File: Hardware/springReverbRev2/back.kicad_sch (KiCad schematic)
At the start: 55 parts, among them IC102 TL074, IC103 TL074, J901 AudioJack2_SwitchT, J902 AudioJack2, J903 AudioJack2, J904 AudioJack2, J905 AudioJack2_SwitchT, J906 AudioJack2, J917 DIP-8, J919 DIP-14, J920 DIP-14, U7 NE5532, U901 L78L05_TO92, X101 RCA, X102 RCA

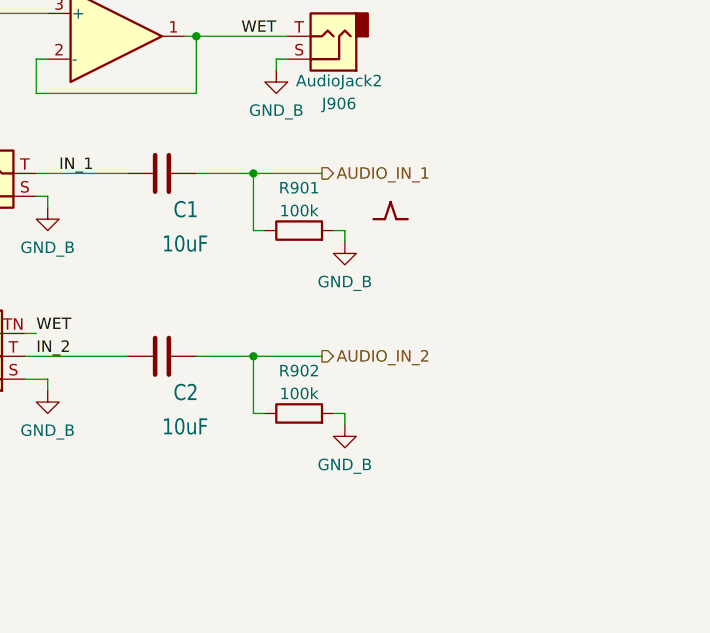
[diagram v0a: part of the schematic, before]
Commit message: Restore R4 and R5 references; change C1 and C2 values; mark R5 to omit; README list of changes
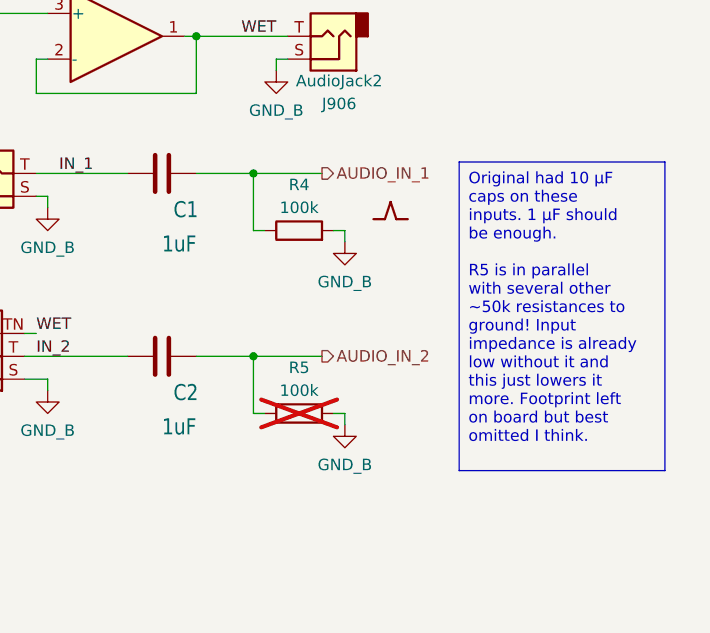
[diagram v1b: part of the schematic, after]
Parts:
- C1, C2: value 10uF -> 1uF; footprint AO_tht:C_Radial_D8.0mm_H11.5mm_P3.50mm -> AO_tht:C_Rect_L7.2mm_W7.2mm_P5.00mm_FKS2_FKP2_MKS2_MKP2
- R5: renamed from R902; now not fitted
- renumbered R901 to R4
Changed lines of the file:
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@@
     (fill (type none))
+  )
+  (text_box "Original had 10 µF caps on these inputs. 1 µF should be enough.\n\nR5 is in parallel with several other ~50k resistances to ground! Input impedance is already low without it and this just lowers it more. Footprint left on board but best omitted I think."
+    (at 243.84 135.89 0) (size 22.86 34.29)
+    (stroke (width 0) (type default))
+    (fill (type none))
+    (effects (font (size 1.27 1.27)) (justify left top))
   )
   (text "Reverb Board" (at 177.8 26.67 0)
@@
   )
   (symbol (lib_id "AO_symbols:R") (at 226.06 163.83 90) (unit 1)
-    (in_bom yes) (on_board yes) (dnp no) (fields_autoplaced)
-    (property "Reference" "R902" (at 226.06 159.1142 90)
-      (effects (font (size 1.27 1.27)))
-    )
-    (property "Value" "100k" (at 226.06 161.6511 90)
+    (in_bom yes) (on_board yes) (dnp yes) (fields_autoplaced)
+    (property "Reference" "R5" (at 226.06 158.75 90)
+      (effects (font (size 1.27 1.27)))
+    )
+    (property "Value" "100k" (at 226.06 161.29 90)
       (effects (font (size 1.27 1.27)))
     )
@@
       (project "springReverbRev2"
         (path "/7cc2117a-75f3-473b-aa3c-f6f0c8514e37/cb7e7ca4-1a75-4992-9aba-d7df48630a9d"
-          (reference "R902") (unit 1)
+          (reference "R5") (unit 1)
         )
       )
@@
     )
   )
-  (symbol (lib_id "AO_symbols:C") (at 210.82 157.48 270) (unit 1)
-    (in_bom yes) (on_board yes) (dnp no)
-    (property "Reference" "C2" (at 212.09 162.56 90)
-      (effects (font (size 1.778 1.5113)) (justify left bottom))
-    )
-    (property "Value" "10uF" (at 210.82 166.37 90)
-      (effects (font (size 1.778 1.5113)) (justify left bottom))
-    )
-    (property "Footprint" "AO_tht:C_Radial_D8.0mm_H11.5mm_P3.50mm" (at 207.01 158.4452 0)
-      (effects (font (size 1.27 1.27)) hide)
-    )
-    (property "Datasheet" "" (at 210.82 157.48 0)
-      (effects (font (size 1.27 1.27)) hide)
-    )
-    (property "Vendor" "Tayda" (at 210.82 157.48 0)
-      (effects (font (size 1.27 1.27)) hide)
-    )
-    (property "Description" "Unpolarized electrolytic capacitor" (at 210.82 157.48 0)
-      (effects (font (size 1.27 1.27)) hide)
-    )
-    (property "Manufacturer" "" (at 210.82 157.48 0)
-      (effects (font (size 1.27 1.27)) hide)
-    )
-    (property "Part" "" (at 210.82 157.48 0)
-      (effects (font (size 1.27 1.27)) hide)
-    )
-    (pin "1")
-    (pin "2")
-    (instances
-      (project "springReverbRev2"
-        (path "/7cc2117a-75f3-473b-aa3c-f6f0c8514e37/cb7e7ca4-1a75-4992-9aba-d7df48630a9d"
-          (reference "C2") (unit 1)
-        )
-      )
-    )
-  )
   (symbol (lib_id "aaaSpringReverb:GND_B") (at 39.37 187.96 0) (unit 1)
     (in_bom yes) (on_board yes) (dnp no) (fields_autoplaced)
@@
       (effects (font (size 1.778 1.5113)) (justify left bottom))
     )
-    (property "Value" "10uF" (at 210.82 146.05 90)
+    (property "Value" "1uF" (at 210.82 146.05 90)
       (effects (font (size 1.778 1.5113)) (justify left bottom))
     )
-    (property "Footprint" "AO_tht:C_Radial_D8.0mm_H11.5mm_P3.50mm" (at 207.01 138.1252 0)
+    (property "Footprint" "AO_tht:C_Rect_L7.2mm_W7.2mm_P5.00mm_FKS2_FKP2_MKS2_MKP2" (at 207.01 138.1252 0)
       (effects (font (size 1.27 1.27)) hide)
     )
@@
     )
   )
+  (symbol (lib_id "AO_symbols:C") (at 210.82 157.48 270) (unit 1)
+    (in_bom yes) (on_board yes) (dnp no)
+    (property "Reference" "C2" (at 212.09 162.56 90)
+      (effects (font (size 1.778 1.5113)) (justify left bottom))
+    )
+    (property "Value" "1uF" (at 210.82 166.37 90)
+      (effects (font (size 1.778 1.5113)) (justify left bottom))
+    )
+    (property "Footprint" "AO_tht:C_Rect_L7.2mm_W7.2mm_P5.00mm_FKS2_FKP2_MKS2_MKP2" (at 207.01 158.4452 0)
+      (effects (font (size 1.27 1.27)) hide)
+    )
+    (property "Datasheet" "" (at 210.82 157.48 0)
+      (effects (font (size 1.27 1.27)) hide)
+    )
+    (property "Vendor" "Tayda" (at 210.82 157.48 0)
+      (effects (font (size 1.27 1.27)) hide)
+    )
+    (property "Description" "Unpolarized electrolytic capacitor" (at 210.82 157.48 0)
+      (effects (font (size 1.27 1.27)) hide)
+    )
+    (property "Manufacturer" "" (at 210.82 157.48 0)
+      (effects (font (size 1.27 1.27)) hide)
+    )
+    (property "Part" "" (at 210.82 157.48 0)
+      (effects (font (size 1.27 1.27)) hide)
+    )
+    (pin "1")
+    (pin "2")
+    (instances
+      (project "springReverbRev2"
+        (path "/7cc2117a-75f3-473b-aa3c-f6f0c8514e37/cb7e7ca4-1a75-4992-9aba-d7df48630a9d"
+          (reference "C2") (unit 1)
+        )
+      )
+    )
+  )
   (symbol (lib_id "aaaSpringReverb:GND_B") (at 198.12 161.29 0) (unit 1)
     (in_bom yes) (on_board yes) (dnp no) (fields_autoplaced)
@@
   (symbol (lib_id "AO_symbols:R") (at 226.06 143.51 90) (unit 1)
     (in_bom yes) (on_board yes) (dnp no) (fields_autoplaced)
-    (property "Reference" "R901" (at 226.06 138.7942 90)
-      (effects (font (size 1.27 1.27)))
-    )
-    (property "Value" "100k" (at 226.06 141.3311 90)
+    (property "Reference" "R4" (at 226.06 138.43 90)
+      (effects (font (size 1.27 1.27)))
+    )
+    (property "Value" "100k" (at 226.06 140.97 90)
       (effects (font (size 1.27 1.27)))
     )
@@
       (project "springReverbRev2"
         (path "/7cc2117a-75f3-473b-aa3c-f6f0c8514e37/cb7e7ca4-1a75-4992-9aba-d7df48630a9d"
-          (reference "R901") (unit 1)
-        )
-      )
+          (reference "R4") (unit 1)
+        )
+      )

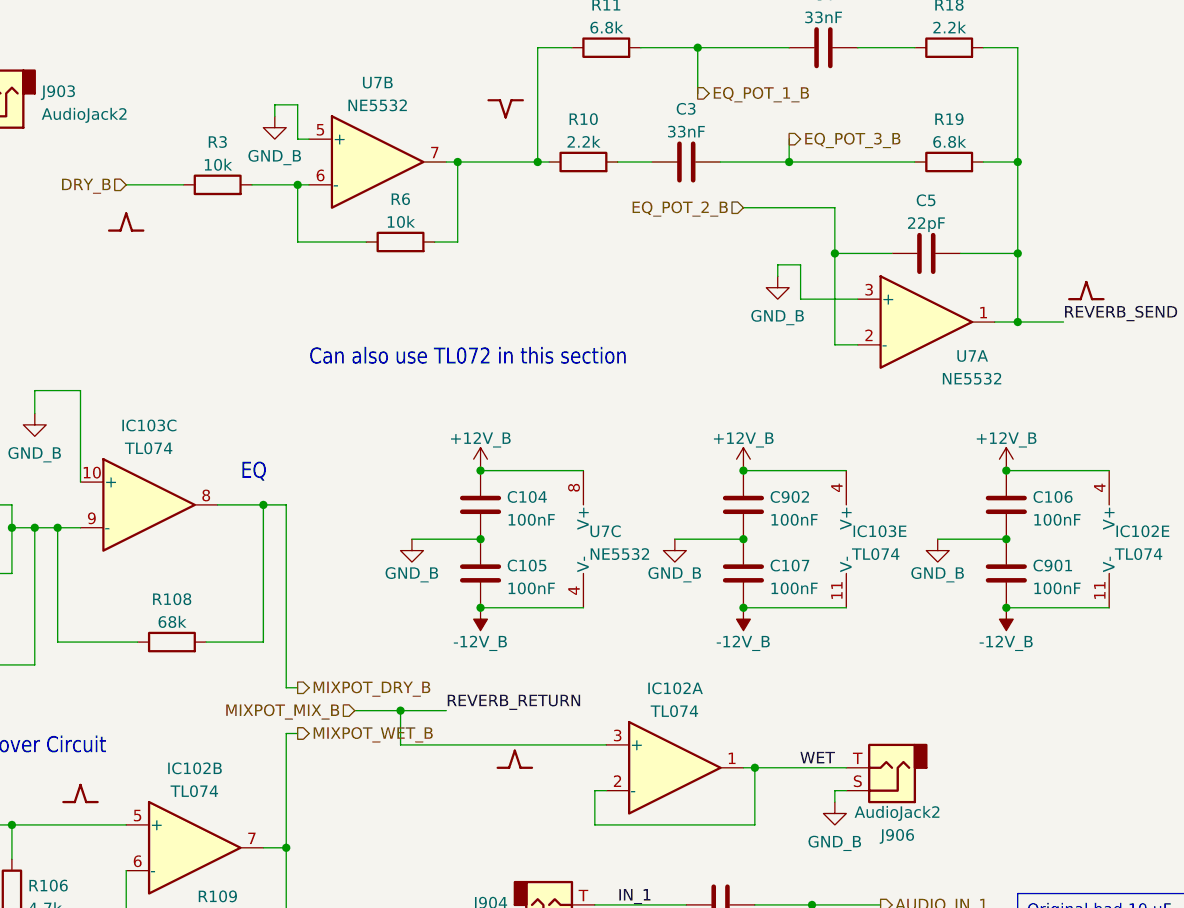
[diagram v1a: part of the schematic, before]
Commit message: Docs; make LED position consistent
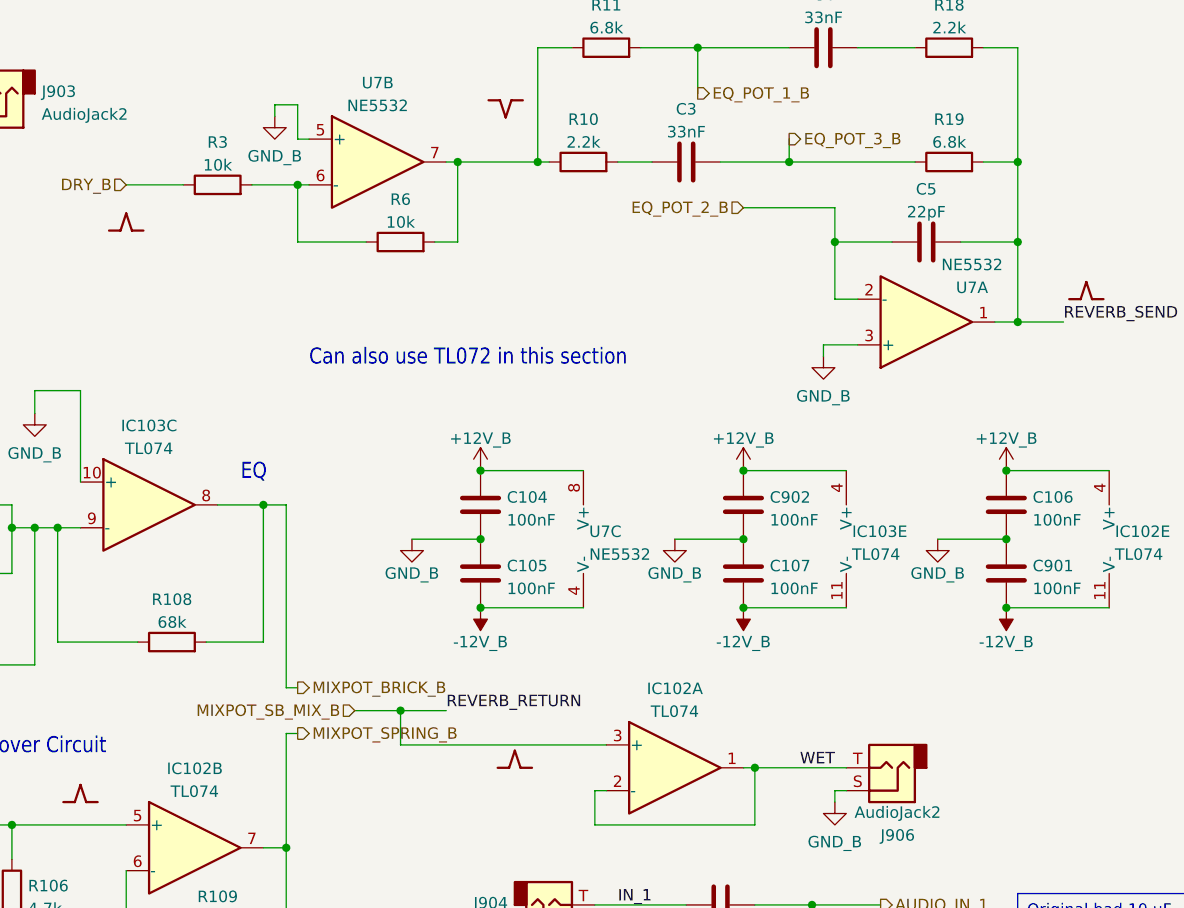
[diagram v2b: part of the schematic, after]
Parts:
- Z$102: Manufacturer (none) -> Belton Accutronics; Part (none) -> BTDR-2H
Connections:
- net MIXPOT_DRY_B renamed MIXPOT_BRICK_B
- net MIXPOT_MIX_B renamed MIXPOT_SB_MIX_B
- net MIXPOT_WET_B renamed MIXPOT_SPRING_B
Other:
- moved on the sheet: C5

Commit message: Use open not bridged jumper
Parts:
- SJ101: footprint Jumper:SolderJumper-2_P1.3mm_Bridged_RoundedPad1.0x1.5mm -> Jumper:SolderJumper-2_P1.3mm_Open_RoundedPad1.0x1.5mm
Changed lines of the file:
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@@
       (effects (font (size 1.27 1.27)))
     )
-    (property "Footprint" "Jumper:SolderJumper-2_P1.3mm_Bridged_RoundedPad1.0x1.5mm" (at 119.38 110.49 0)
+    (property "Footprint" "Jumper:SolderJumper-2_P1.3mm_Open_RoundedPad1.0x1.5mm" (at 119.38 110.49 0)
       (effects (font (size 1.27 1.27)) hide)
     )
